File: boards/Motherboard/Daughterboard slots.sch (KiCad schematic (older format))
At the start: 6 parts, among them P701 SLOT_A, P702 SLOT_D, P703 SLOT_B, P704 SLOT_E, P705 SLOT_C, P706 SLOT_F

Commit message: Changed power pin/port names
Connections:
- net ID_GND is gone; now on net GND: P701.13 (P13), P701.14, P701.15, P702.13 (P13), P702.15, P702.16, P703.13 (P13), P703.14, P703.16, P704.13 (P13), P704.15, P705.13 (P13), P705.14, P706.13 (P13), P706.16
- net GND: no longer P701.8 (P8), P702.8 (P8), P703.8 (P8), P704.8 (P8), P705.8 (P8), P706.8 (P8)
- net ID_3V3 renamed VCC_3V3
- new net GND_ISO: P701.8 (P8), P702.8 (P8), P703.8 (P8), P704.8 (P8), P705.8 (P8), P706.8 (P8)
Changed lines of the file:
@@
 VCC_5V_ISO
 Text HLabel 3250 2600 0    60   Input ~ 0
-GND
+GND_ISO
 Text HLabel 3250 2800 0    60   BiDi ~ 0
 ID_SDA
@@
 ID_SCL
 Text HLabel 2900 3000 0    60   Input ~ 0
-ID_3V3
+VCC_3V3
 Text HLabel 2900 3100 0    60   Input ~ 0
-ID_GND
+GND
 Text HLabel 5700 2000 0    60   Output ~ 0
 RX1
@@
 VCC_5V_ISO
 Text HLabel 5700 2600 0    60   Input ~ 0
-GND
+GND_ISO
 Text HLabel 8450 2000 0    60   Output ~ 0
 RX2
@@
 VCC_5V_ISO
 Text HLabel 8450 2600 0    60   Input ~ 0
-GND
+GND_ISO
 Text HLabel 3250 4600 0    60   Output ~ 0
 RX3
@@
 VCC_5V_ISO
 Text HLabel 3250 5200 0    60   Input ~ 0
-GND
+GND_ISO
 Text HLabel 5700 4600 0    60   Output ~ 0
 RX4
@@
 VCC_5V_ISO
 Text HLabel 5700 5200 0    60   Input ~ 0
-GND
+GND_ISO
 Text HLabel 8450 4600 0    60   Output ~ 0
 RX5
@@
 VCC_5V_ISO
 Text HLabel 8450 5200 0    60   Input ~ 0
-GND
+GND_ISO
 NoConn ~ 3400 2700
 NoConn ~ 5850 2700
@@
 ID_SCL
 Text HLabel 5350 3000 0    60   Input ~ 0
-ID_3V3
+VCC_3V3
 Text HLabel 5350 3100 0    60   Input ~ 0
-ID_GND
+GND
 Text HLabel 8450 2800 0    60   BiDi ~ 0
 ID_SDA
@@
 ID_SCL
 Text HLabel 8100 3000 0    60   Input ~ 0
-ID_3V3
+VCC_3V3
 Text HLabel 8100 3100 0    60   Input ~ 0
-ID_GND
+GND
 Text HLabel 3250 5400 0    60   BiDi ~ 0
 ID_SDA
@@
 ID_SCL
 Text HLabel 2900 5600 0    60   Input ~ 0
-ID_3V3
+VCC_3V3
 Text HLabel 2900 5700 0    60   Input ~ 0
-ID_GND
+GND
 Text HLabel 5700 5400 0    60   BiDi ~ 0
 ID_SDA
@@
 ID_SCL
 Text HLabel 5350 5600 0    60   Input ~ 0
-ID_3V3
+VCC_3V3
 Text HLabel 5350 5700 0    60   Input ~ 0
-ID_GND
+GND
 Text HLabel 8450 5400 0    60   BiDi ~ 0
 ID_SDA
@@
 ID_SCL
 Text HLabel 8100 5600 0    60   Input ~ 0
-ID_3V3
+VCC_3V3
 Text HLabel 8100 5700 0    60   Input ~ 0
-ID_GND
+GND
 Wire Wire Line
 	3400 1900 3250 1900

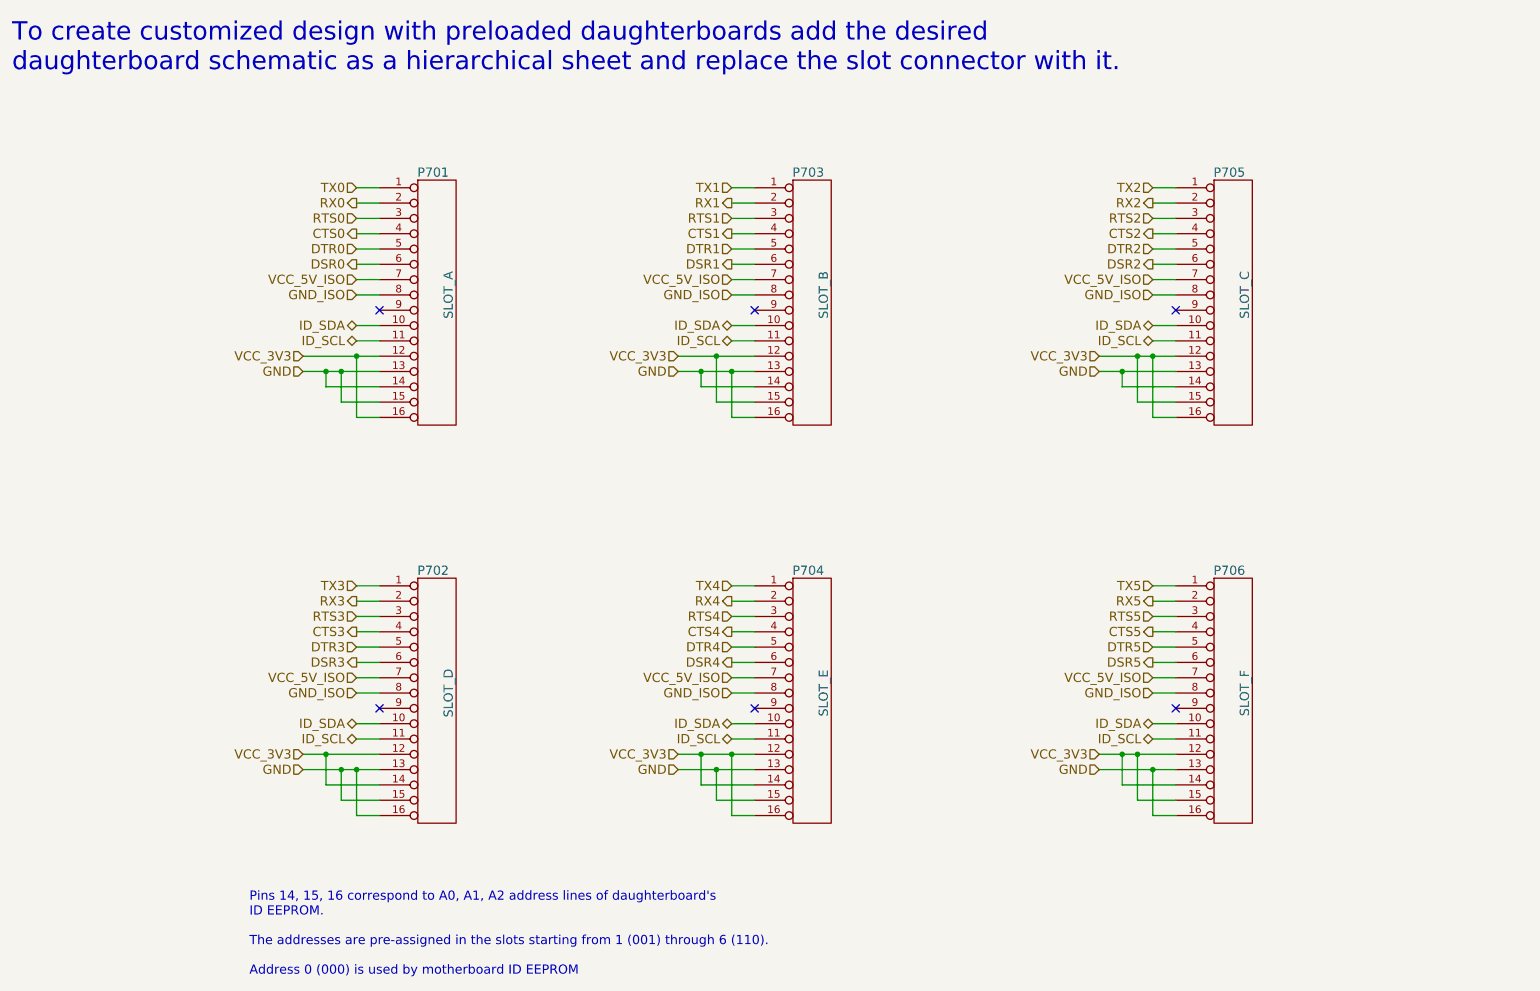
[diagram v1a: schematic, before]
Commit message: Changed daughterboard slots to support Digilent PMOD and changed label names
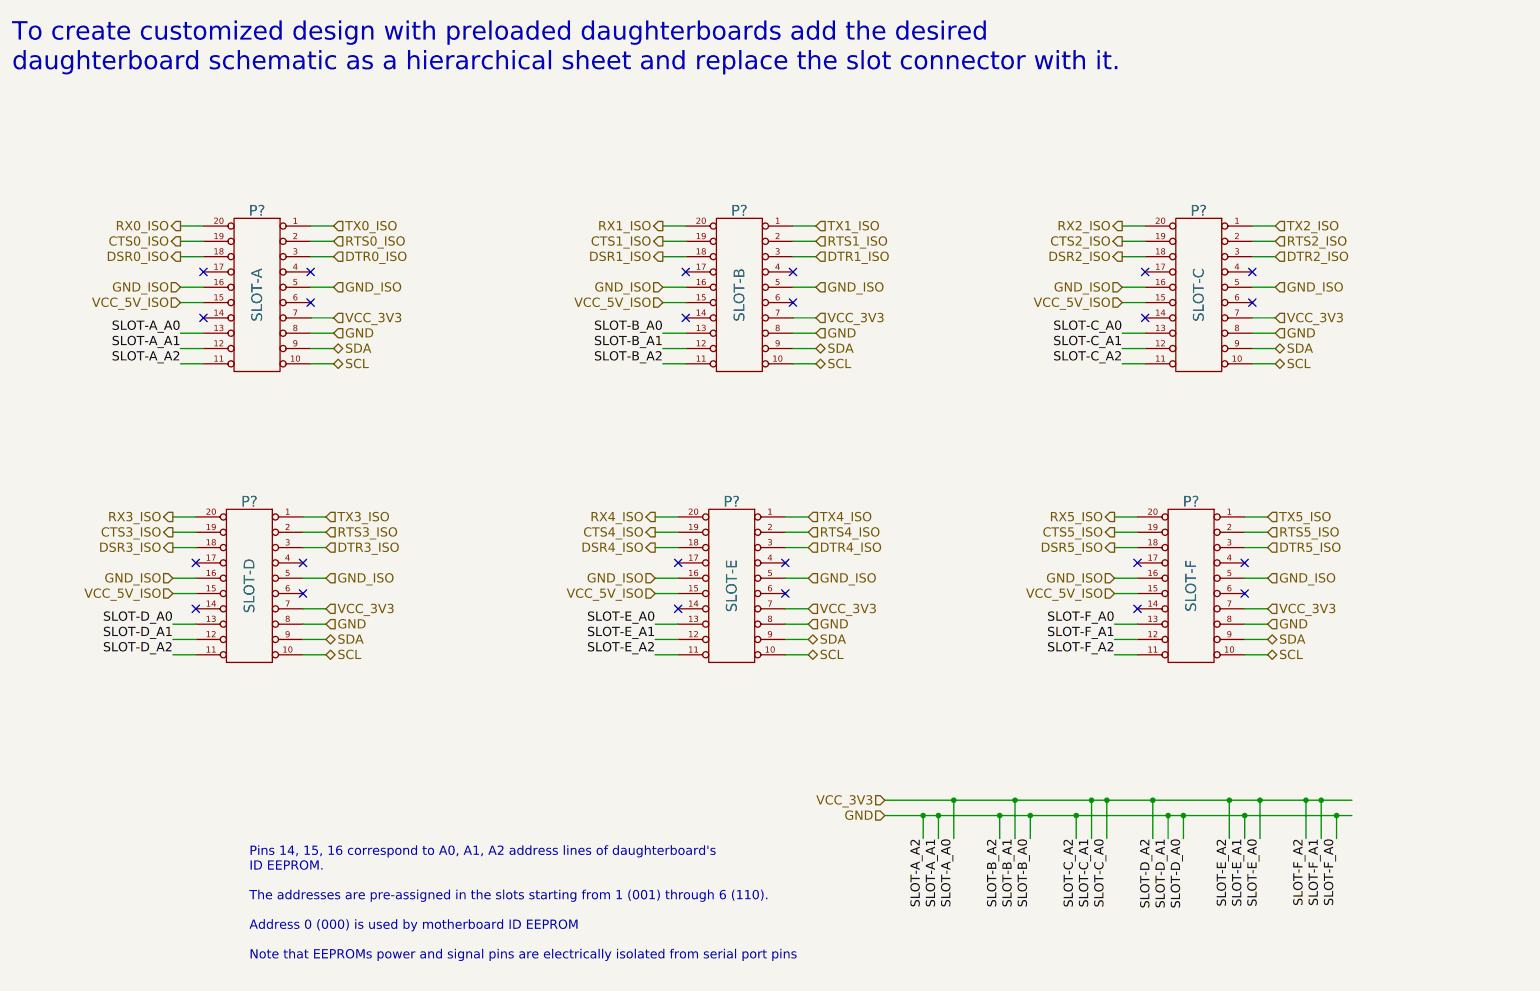
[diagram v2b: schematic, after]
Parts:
- removed P701: SLOT_A, ~, symbol CONN_16
- removed P702: SLOT_D, ~, symbol CONN_16
- removed P703: SLOT_B, ~, symbol CONN_16
- removed P704: SLOT_E, ~, symbol CONN_16
- removed P705: SLOT_C, ~, symbol CONN_16
- removed P706: SLOT_F, ~, symbol CONN_16
- added P?: SLOT-A, symbol DIL20
- added P?: SLOT-B, symbol DIL20
- added P?: SLOT-C, symbol DIL20
- added P?: SLOT-D, symbol DIL20
- added P?: SLOT-E, symbol DIL20
- added P?: SLOT-F, symbol DIL20
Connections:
- net GND: now also P?.11 (P11), P?.11 (P11), P?.11 (P11), P?.12 (P12), P?.12 (P12), P?.12 (P12), P?.13 (P13), P?.13 (P13), P?.13 (P13), P?.8 (P8), P?.8 (P8), P?.8 (P8), P?.8 (P8), P?.8 (P8), P?.8 (P8)
- net GND_ISO: now also P?.16 (P16), P?.16 (P16), P?.16 (P16), P?.16 (P16), P?.16 (P16), P?.16 (P16), P?.5 (P5), P?.5 (P5), P?.5 (P5), P?.5 (P5), P?.5 (P5), P?.5 (P5)
- net VCC_3V3: now also P?.11 (P11), P?.11 (P11), P?.11 (P11), P?.12 (P12), P?.12 (P12), P?.12 (P12), P?.13 (P13), P?.13 (P13), P?.13 (P13), P?.7 (P7), P?.7 (P7), P?.7 (P7), P?.7 (P7), P?.7 (P7), P?.7 (P7)
- net VCC_5V_ISO: now also P?.15 (P15), P?.15 (P15), P?.15 (P15), P?.15 (P15), P?.15 (P15), P?.15 (P15)
- new net CTS0_ISO: P?.19 (P19)
- new net CTS1_ISO: P?.19 (P19)
- new net CTS2_ISO: P?.19 (P19)
- new net CTS3_ISO: P?.19 (P19)
- new net CTS4_ISO: P?.19 (P19)
- new net CTS5_ISO: P?.19 (P19)
- new net DSR0_ISO: P?.18 (P18)
- new net DSR1_ISO: P?.18 (P18)
- new net DSR2_ISO: P?.18 (P18)
- new net DSR3_ISO: P?.18 (P18)
- new net DSR4_ISO: P?.18 (P18)
- new net DSR5_ISO: P?.18 (P18)
- new net DTR0_ISO: P?.3 (P3)
- new net DTR1_ISO: P?.3 (P3)
- new net DTR2_ISO: P?.3 (P3)
- new net DTR3_ISO: P?.3 (P3)
- new net DTR4_ISO: P?.3 (P3)
- new net DTR5_ISO: P?.3 (P3)
- new net RTS0_ISO: P?.2 (P2)
- new net RTS1_ISO: P?.2 (P2)
- new net RTS2_ISO: P?.2 (P2)
- new net RTS3_ISO: P?.2 (P2)
- new net RTS4_ISO: P?.2 (P2)
- new net RTS5_ISO: P?.2 (P2)
- new net RX0_ISO: P?.20 (P20)
- new net RX1_ISO: P?.20 (P20)
- new net RX2_ISO: P?.20 (P20)
- new net RX3_ISO: P?.20 (P20)
- new net RX4_ISO: P?.20 (P20)
- new net RX5_ISO: P?.20 (P20)
- new net SCL: P?.10 (P10), P?.10 (P10), P?.10 (P10), P?.10 (P10), P?.10 (P10), P?.10 (P10)
- new net SDA: P?.9 (P9), P?.9 (P9), P?.9 (P9), P?.9 (P9), P?.9 (P9), P?.9 (P9)
- new net TX0_ISO: P?.1 (P1)
- new net TX1_ISO: P?.1 (P1)
- new net TX2_ISO: P?.1 (P1)
- new net TX3_ISO: P?.1 (P1)
- new net TX4_ISO: P?.1 (P1)
- new net TX5_ISO: P?.1 (P1)
- no-connect marks 6 -> 24
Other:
- note added: "Pins 14, 15, 16 correspond to A0, A1, A2 address lines of daughterboard's \nID EEPROM. \n\nThe addresses are pre-assigned in the slots starting from 1 (001) through 6 (110).\n\nAddress 0 (000) is used by motherboard ID EEPROM\n\nNote that EEPROMs power and signal pins are electrically isolated from serial port pins"
- note removed: "Pins 14, 15, 16 correspond to A0, A1, A2 address lines of daughterboard's \nID EEPROM. \n\nThe addresses are pre-assigned in the slots starting from 1 (001) through 6 (110).\n\nAddress 0 (000) is used by motherboard ID EEPROM"
